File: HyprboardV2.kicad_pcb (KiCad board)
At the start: 2 copper layers, 21 x 51 mm, 33 parts, among them J1 USB_C_Receptacle_USB2.0_14P, J2 Conn_01x20, J3 Conn_01x20, J4 Conn_01x03, SW1 SW_Push, U1 RP2040, U2 NCP1117-3.3_SOT223, U3 W25Q128JVS, Y1 12 MHz

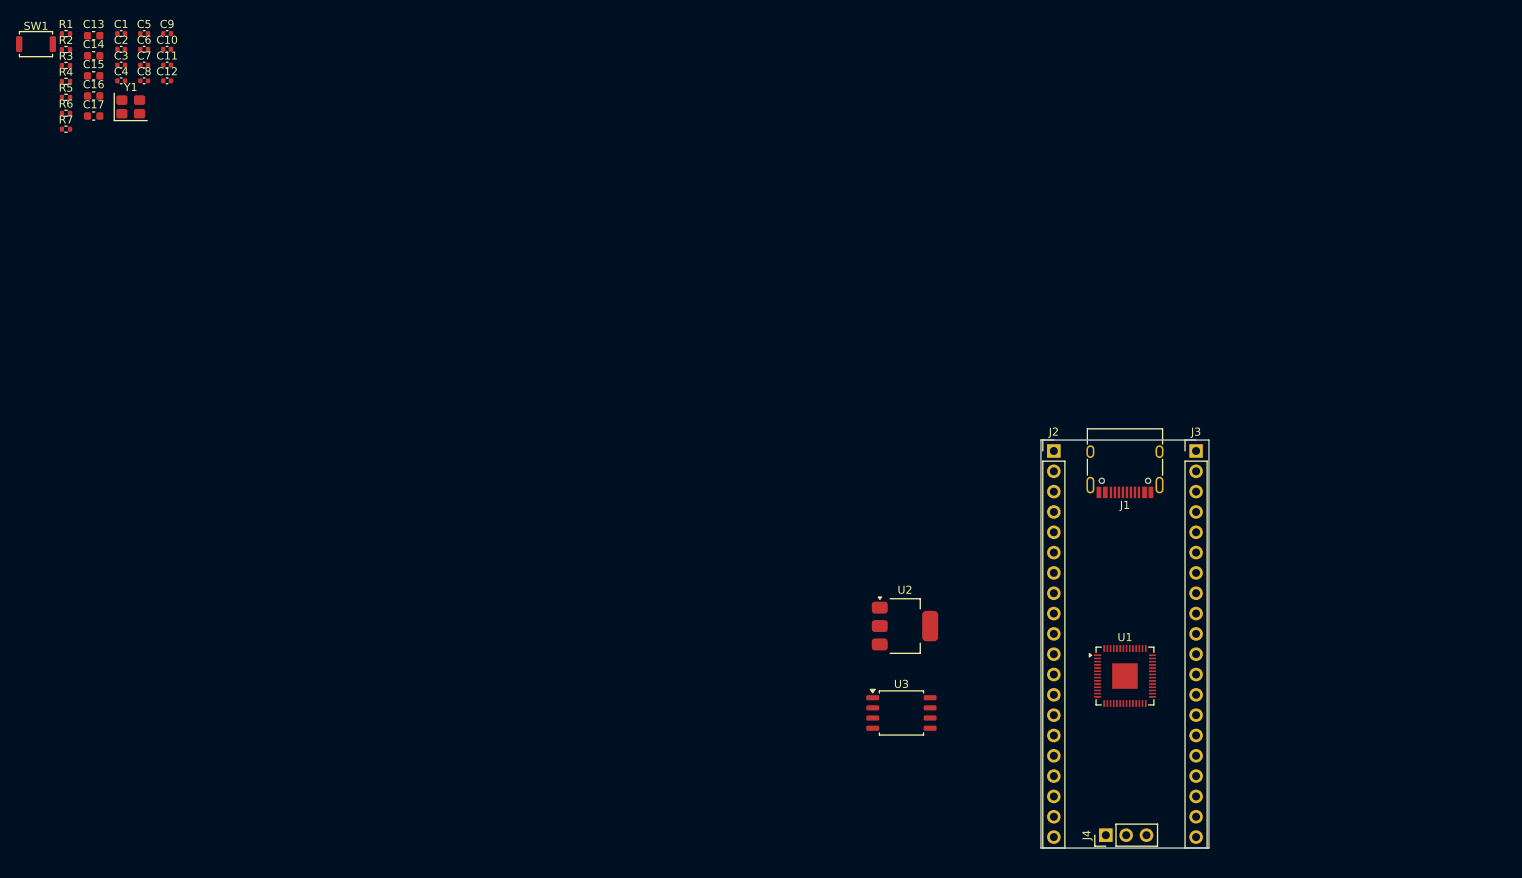
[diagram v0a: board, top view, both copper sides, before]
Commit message: Position 2/3rd of the components
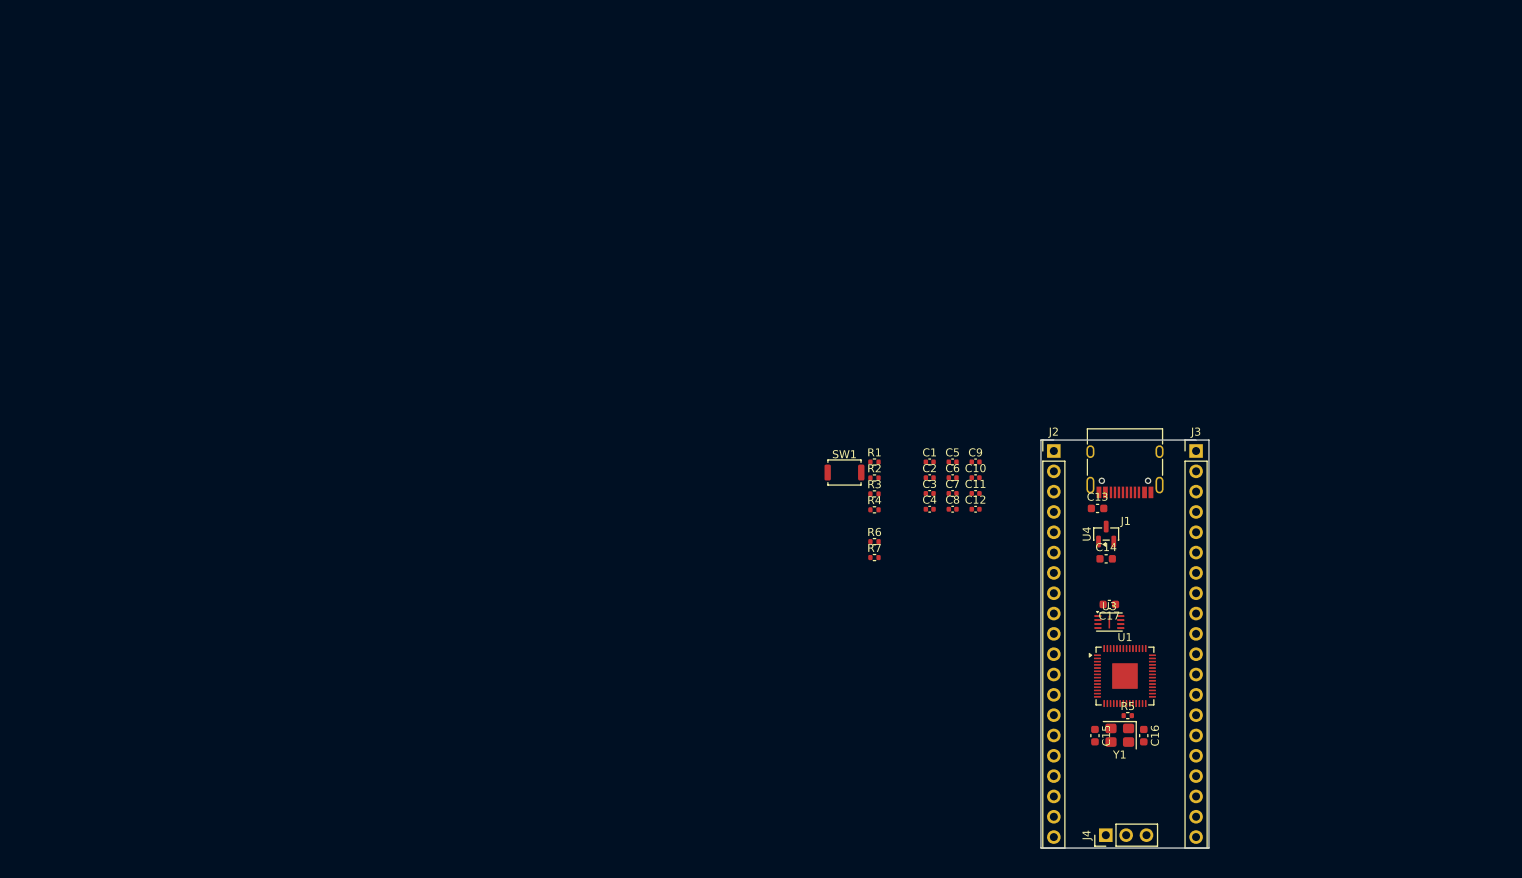
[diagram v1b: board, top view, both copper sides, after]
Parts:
- removed U2: NCP1117-3.3_SOT223, Package_TO_SOT_SMD:SOT-223-3_TabPin2
- added U4: MCP1700x-330xxTT, Package_TO_SOT_SMD:SOT-23, F.Cu at (169.0, 84.0)
- U3: value W25Q128JVS -> W25Q16JVZPIQ TR; footprint Package_SO:SOIC-8_5.3x5.3mm_P1.27mm -> Package_SON:Winbond_USON-8-1EP_3x2mm_P0.5mm_EP0.2x1.6mm
- moved C16 153.7 mm to (173.7, 109.2), turned to -90 degrees
- moved R5 153.6 mm to (171.7, 106.7)
- moved C15 149.9 mm to (167.6, 109.2), turned to -90 degrees
- moved Y1 146.5 mm to (170.7, 109.2), turned to 180 degrees
- moved C14 141.3 mm to (169.0, 87.1)
- moved C17 140.9 mm to (169.4, 92.8), turned to 180 degrees
- moved C13 138.7 mm to (167.9, 80.8)
- moved C1 114.4 mm to (146.9, 75.0)
- moved C10 114.4 mm to (152.7, 77.0)
- moved C11 114.4 mm to (152.7, 78.9)
- moved C12 114.4 mm to (152.7, 80.9)
- moved C2 114.4 mm to (146.9, 77.0)
- moved C3 114.4 mm to (146.9, 78.9)
- moved C4 114.4 mm to (146.9, 80.9)
- moved C5 114.4 mm to (149.8, 75.0)
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
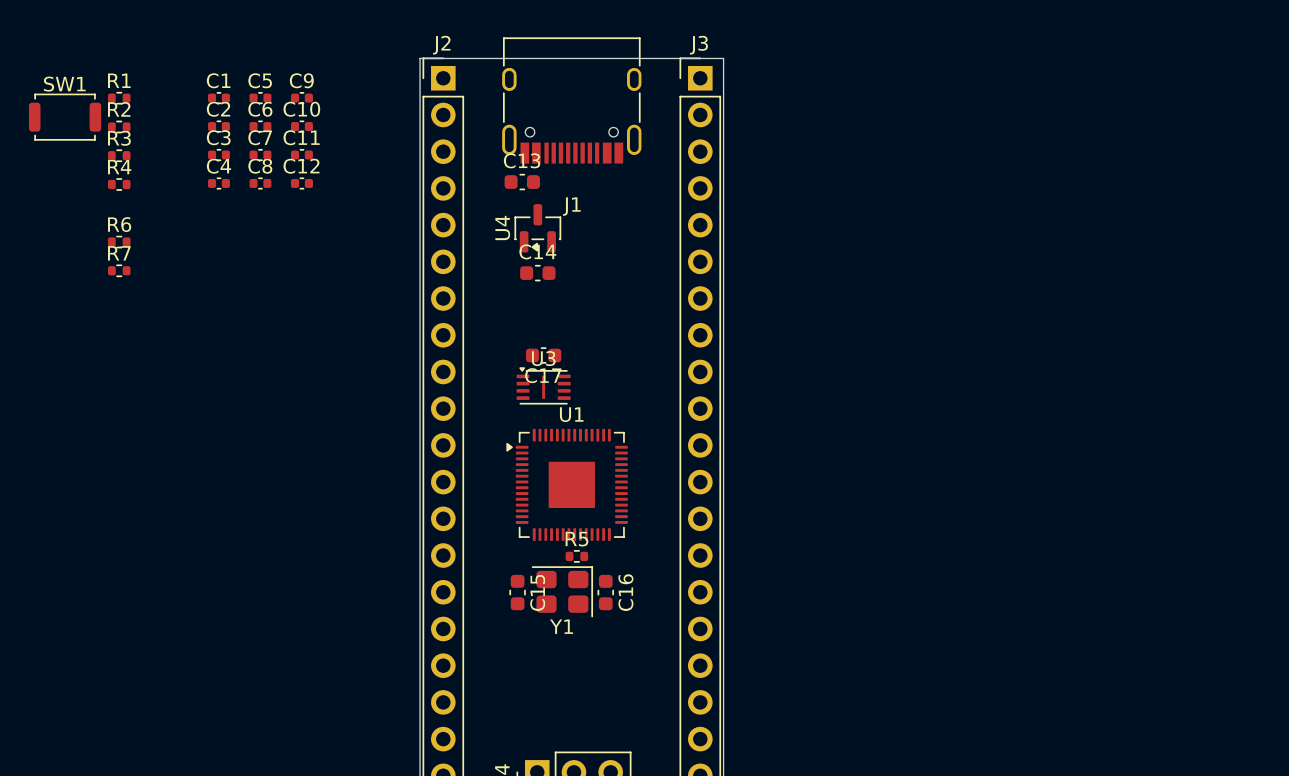
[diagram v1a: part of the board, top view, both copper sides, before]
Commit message: Almost dont placements, ill start routing next and do the rest simulatneously
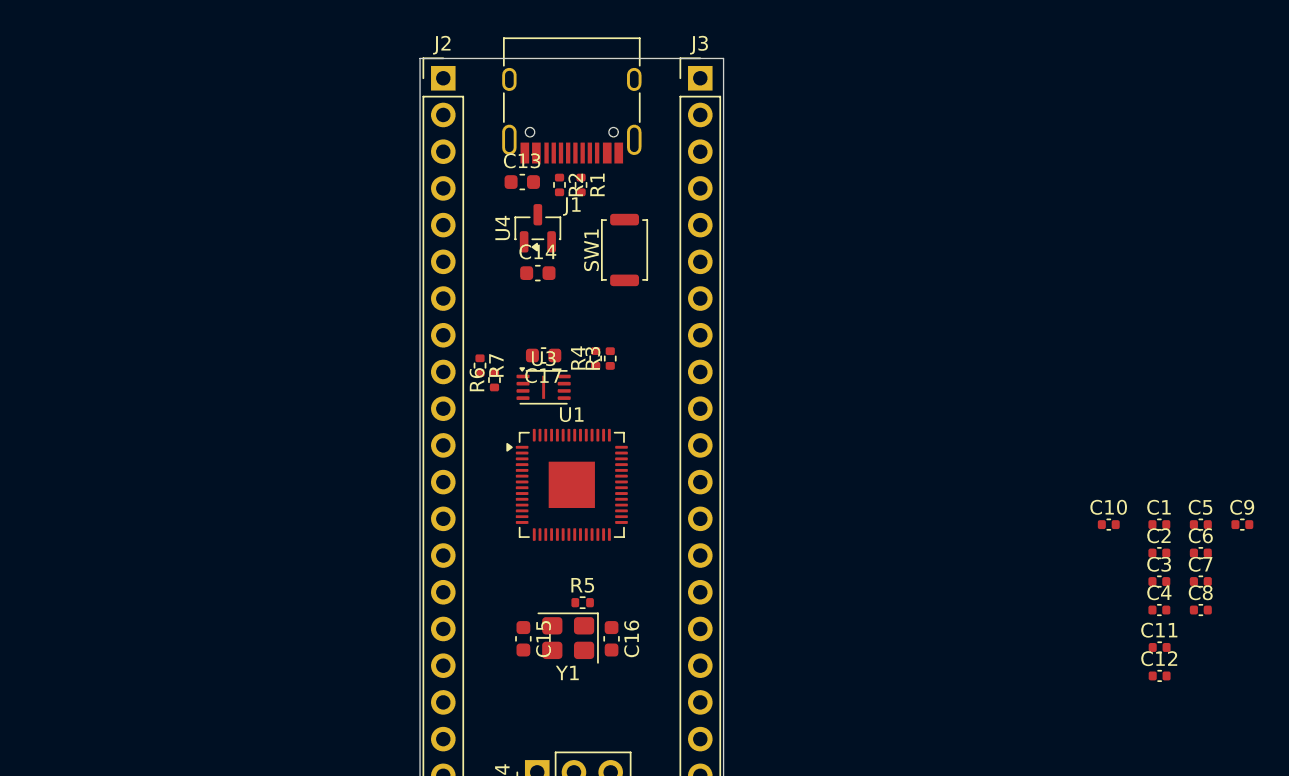
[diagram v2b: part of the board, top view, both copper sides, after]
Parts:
- moved C1 71.4 mm to (212.0, 104.5)
- moved C2 71.4 mm to (212.0, 106.5)
- moved C5 71.4 mm to (214.9, 104.5)
- moved C6 71.4 mm to (214.9, 106.5)
- moved C9 71.4 mm to (217.7, 104.5)
- moved C3 71.4 mm to (212.0, 108.4)
- moved C4 71.4 mm to (212.0, 110.4)
- moved C7 71.4 mm to (214.9, 108.4)
- moved C8 71.4 mm to (214.9, 110.4)
- moved C11 68.4 mm to (212.0, 113.0)
- moved C12 68.4 mm to (212.0, 115.0)
- moved C10 62.2 mm to (208.5, 104.5)
- moved SW1 39.8 mm to (175.0, 85.5), turned to 90 degrees
- moved R3 36.8 mm to (174.0, 93.0), turned to 90 degrees
- moved R4 35.1 mm to (173.0, 93.0), turned to 90 degrees
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
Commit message: DONE WITH THE ROUTINGGGgit add .! checkout stasis's journal for info
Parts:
- removed U3: W25Q16JVZPIQ TR, Package_SON:Winbond_USON-8-1EP_3x2mm_P0.5mm_EP0.2x1.6mm
- added U2: MCP1700x-330xxTT, Package_TO_SOT_SMD:SOT-23, F.Cu at (127.9, 85.4)
- C17: footprint Capacitor_SMD:C_0603_1608Metric -> Capacitor_SMD:C_0402_1005Metric
- R6: value 10K -> 1K
- R7: value 1K -> 10K
- U4: value MCP1700x-330xxTT -> W25Q16JVZPIQ TR; footprint Package_TO_SOT_SMD:SOT-23 -> Package_SON:Winbond_USON-8-1EP_3x2mm_P0.5mm_EP0.2x1.6mm
- moved C3 87.2 mm to (124.9, 104.6), turned to 180 degrees
- moved C4 87.2 mm to (125.5, 99.8), turned to 180 degrees
- moved C6 84.2 mm to (131.4, 95.3), turned to 90 degrees
- moved C12 84.0 mm to (130.4, 95.3), turned to 90 degrees
- moved C7 83.7 mm to (132.4, 94.6), turned to 90 degrees
- moved C9 81.4 mm to (136.4, 104.3)
- moved C5 81.0 mm to (134.1, 98.5), turned to 90 degrees
- moved C11 80.3 mm to (133.1, 98.2), turned to 90 degrees
- moved C8 80.2 mm to (135.4, 99.9)
- moved C2 79.9 mm to (132.2, 109.0), turned to -90 degrees
- moved C1 76.7 mm to (135.6, 98.3), turned to 45 degrees
- moved C10 75.4 mm to (133.2, 109.0), turned to -90 degrees
- moved U4 43.4 mm to (127.2, 95.7), turned to 0 degrees
- moved R1 43.0 mm to (129.0, 82.7)
- moved R4 42.3 mm to (131.0, 97.8), turned to -90 degrees
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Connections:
- C13 pad 2: Net-(C13-Pad2) -> GND
- C14 pad 2: Net-(C13-Pad2) -> GND
- J1 pad A6: USD_D+ -> USB_D+
- J1 pad A7: USD_D- -> USB_D-
- J1 pad B6: USD_D+ -> USB_D+
- J1 pad B7: USD_D- -> USB_D-
- R1 pad 1: Net-(J1-CC1) -> Net-(J1-CC2)
- R2 pad 1: Net-(J1-CC2) -> Net-(J1-CC1)
- R3 pad 1: Net-(U1-USB_DM) -> USB_D-
- R3 pad 2: USD_D+ -> Net-(U1-USB_DM)
- R4 pad 1: Net-(U1-USB_DP) -> USB_D+
- R4 pad 2: USD_D- -> Net-(U1-USB_DP)
- R6 pad 1: +3V3 -> Net-(R6-Pad1)
- R7 pad 1: Net-(R7-Pad1) -> +3V3
- SW1 pad 2: Net-(R7-Pad1) -> Net-(R6-Pad1)
- U4 pad 1: GND -> QSPI_SS
- U4 pad 2: +3V3 -> QSPI_SD1
- U4 pad 3: VBUS -> QSPI_SD2
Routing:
- net +3V3: track 0.00 -> 80.9 mm, vias 0 -> 4
- net +1V1: track 0.00 -> 30.9 mm, vias 0 -> 3
- net GPIO0: track 0.00 -> 28.7 mm, vias 0 -> 1
- net GPIO1: track 0.00 -> 26.9 mm, vias 0 -> 1
- net GPIO29_ADC3: track 0.00 -> 26.4 mm, vias 0 -> 1
- net GND: track 0.00 -> 23.8 mm, vias 0 -> 36
- net GPIO2: track 0.00 -> 22.4 mm, vias 0 -> 1
- net GPIO28_ADC2: track 0.00 -> 22.2 mm, vias 0 -> 1
- net USB_D+: track 0.00 -> 22.1 mm
- net USB_D-: track 0.00 -> 22.0 mm
- net GPIO16: track 0.00 -> 22.0 mm
- net GPIO15: track 0.00 -> 21.8 mm
- net GPIO3: track 0.00 -> 20.7 mm
- net SWCLK: track 0.00 -> 20.6 mm, vias 0 -> 1
- net VBUS: track 0.00 -> 20.1 mm
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- added copper zone on B.Cu, net GND
- added copper zone on F.Cu, net GND
